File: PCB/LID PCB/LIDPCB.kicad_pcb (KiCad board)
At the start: 2 copper layers, 22 x 17 mm, 10 parts, among them J1 POWER/I2C, U1 LTR-329ALS-01, U2 LSM6DSMTR

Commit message: Main pcb reviewed
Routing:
- net /SDA: track 13.5 -> 18.8 mm
- net /SCL: track 17.5 -> 19.0 mm
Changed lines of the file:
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@@
   (segment (start 115.9 114.3) (end 118.5 114.3) (width 0.25) (layer "B.Cu") (net 2))
   (segment (start 102.75 107.175) (end 102.75 104.2875) (width 0.25) (layer "F.Cu") (net 3))
-  (segment (start 117.1 111.1) (end 117.9 111.1) (width 0.2) (layer "F.Cu") (net 4))
-  (segment (start 117.9 111.1) (end 118 111) (width 0.2) (layer "F.Cu") (net 4))
-  (segment (start 118 111) (end 118 113.34) (width 0.25) (layer "F.Cu") (net 4))
+  (segment (start 118 113.34) (end 118 112.8) (width 0.16) (layer "F.Cu") (net 4))
+  (segment (start 117.1 111.1) (end 117.9 111.1) (width 0.16) (layer "F.Cu") (net 4))
+  (segment (start 117.462476 111.9) (end 117.7 111.9) (width 0.16) (layer "F.Cu") (net 4))
+  (segment (start 117.9 111.1) (end 118 111) (width 0.16) (layer "F.Cu") (net 4))
+  (segment (start 118 111.6) (end 118 111.55) (width 0.16) (layer "F.Cu") (net 4))
+  (segment (start 117.7 112.5) (end 117.462476 112.5) (width 0.16) (layer "F.Cu") (net 4))
+  (segment (start 118 111.55) (end 118 111) (width 0.16) (layer "F.Cu") (net 4))
   (via (at 117.1 111.1) (size 0.5) (drill 0.25) (layers "F.Cu" "B.Cu") (net 4))
-  (segment (start 107.75 109) (end 109.3 110.55) (width 0.2) (layer "B.Cu") (net 4))
-  (segment (start 109.3 110.55) (end 113.7 110.55) (width 0.2) (layer "B.Cu") (net 4))
-  (segment (start 115.915686 110.55) (end 116.332843 110.967157) (width 0.2) (layer "B.Cu") (net 4))
-  (segment (start 116.465686 111.1) (end 117.1 111.1) (width 0.2) (layer "B.Cu") (net 4))
-  (segment (start 116.332843 110.967157) (end 116.465686 111.1) (width 0.2) (layer "B.Cu") (net 4))
-  (segment (start 113.7 110.55) (end 115.915686 110.55) (width 0.2) (layer "B.Cu") (net 4))
-  (segment (start 118.5 111.699998) (end 118.5 113.34) (width 0.25) (layer "F.Cu") (net 5))
-  (segment (start 119.299998 111.1) (end 119.199998 111) (width 0.2) (layer "F.Cu") (net 5))
-  (segment (start 119.199998 111) (end 118.5 111.699998) (width 0.25) (layer "F.Cu") (net 5))
-  (segment (start 120 111.1) (end 119.299998 111.1) (width 0.2) (layer "F.Cu") (net 5))
+  (arc (start 117.162476 112.2) (mid 117.250344 111.987868) (end 117.462476 111.9) (width 0.16) (layer "F.Cu") (net 4))
+  (arc (start 117.462476 112.5) (mid 117.250344 112.412132) (end 117.162476 112.2) (width 0.16) (layer "F.Cu") (net 4))
+  (arc (start 117.7 111.9) (mid 117.912132 111.812132) (end 118 111.6) (width 0.16) (layer "F.Cu") (net 4))
+  (arc (start 118 112.8) (mid 117.912132 112.587868) (end 117.7 112.5) (width 0.16) (layer "F.Cu") (net 4))
+  (segment (start 115.75 110.55) (end 115.8 110.55) (width 0.16) (layer "B.Cu") (net 4))
+  (segment (start 114.25 109.876854) (end 114.25 110.25) (width 0.16) (layer "B.Cu") (net 4))
+  (segment (start 114.85 110.25) (end 114.85 109.876854) (width 0.16) (layer "B.Cu") (net 4))
+  (segment (start 115.915686 110.55) (end 116.465686 111.1) (width 0.16) (layer "B.Cu") (net 4))
+  (segment (start 116.465686 111.1) (end 117.1 111.1) (width 0.16) (layer "B.Cu") (net 4))
+  (segment (start 115.8 110.55) (end 115.915686 110.55) (width 0.16) (layer "B.Cu") (net 4))
+  (segment (start 115.45 109.876854) (end 115.45 110.25) (width 0.16) (layer "B.Cu") (net 4))
+  (segment (start 107.75 109) (end 109.3 110.55) (width 0.16) (layer "B.Cu") (net 4))
+  (segment (start 109.3 110.55) (end 112.15 110.55) (width 0.16) (layer "B.Cu") (net 4))
+  (segment (start 113.05 109.876854) (end 113.05 110.25) (width 0.16) (layer "B.Cu") (net 4))
+  (segment (start 112.45 110.25) (end 112.45 109.876854) (width 0.16) (layer "B.Cu") (net 4))
+  (segment (start 113.65 110.25) (end 113.65 109.876854) (width 0.16) (layer "B.Cu") (net 4))
+  (arc (start 114.85 109.876854) (mid 114.937868 109.664722) (end 115.15 109.576854) (width 0.16) (layer "B.Cu") (net 4))
+  (arc (start 114.25 110.25) (mid 114.337868 110.462132) (end 114.55 110.55) (width 0.16) (layer "B.Cu") (net 4))
+  (arc (start 115.45 110.25) (mid 115.537868 110.462132) (end 115.75 110.55) (width 0.16) (layer "B.Cu") (net 4))
+  (arc (start 113.95 109.576854) (mid 114.162132 109.664722) (end 114.25 109.876854) (width 0.16) (layer "B.Cu") (net 4))
+  (arc (start 112.15 110.55) (mid 112.362132 110.462132) (end 112.45 110.25) (width 0.16) (layer "B.Cu") (net 4))
+  (arc (start 113.65 109.876854) (mid 113.737868 109.664722) (end 113.95 109.576854) (width 0.16) (layer "B.Cu") (net 4))
+  (arc (start 112.75 109.576854) (mid 112.962132 109.664722) (end 113.05 109.876854) (width 0.16) (layer "B.Cu") (net 4))
+  (arc (start 112.45 109.876854) (mid 112.537868 109.664722) (end 112.75 109.576854) (width 0.16) (layer "B.Cu") (net 4))
+  (arc (start 113.05 110.25) (mid 113.137868 110.462132) (end 113.35 110.55) (width 0.16) (layer "B.Cu") (net 4))
+  (arc (start 115.15 109.576854) (mid 115.362132 109.664722) (end 115.45 109.876854) (width 0.16) (layer "B.Cu") (net 4))
+  (arc (start 113.35 110.55) (mid 113.562132 110.462132) (end 113.65 110.25) (width 0.16) (layer "B.Cu") (net 4))
+  (arc (start 114.55 110.55) (mid 114.762132 110.462132) (end 114.85 110.25) (width 0.16) (layer "B.Cu") (net 4))
+  (segment (start 118.5 112.9) (end 118.6302 112.7698) (width 0.16) (layer "F.Cu") (net 5))
+  (segment (start 118.6302 112.7698) (end 118.6302 112.4302) (width 0.16) (layer "F.Cu") (net 5))
+  (segment (start 118.7302 111) (end 119.199998 111) (width 0.16) (layer "F.Cu") (net 5))
+  (segment (start 118.6302 111.1) (end 118.7302 111) (width 0.16) (layer "F.Cu") (net 5))
+  (segment (start 119.299998 111.1) (end 119.199998 111) (width 0.16) (layer "F.Cu") (net 5))
+  (segment (start 118.6302 111.2302) (end 118.6302 111.1) (width 0.16) (layer "F.Cu") (net 5))
+  (segment (start 119.18515 111.87525) (end 119.18515 111.8302) (width 0.16) (layer "F.Cu") (net 5))
+  (segment (start 118.6302 111.27525) (end 118.6302 111.2302) (width 0.16) (layer "F.Cu") (net 5))
+  (segment (start 120 111.1) (end 119.299998 111.1) (width 0.16) (layer "F.Cu") (net 5))
+  (segment (start 118.5 113.34) (end 118.5 112.9) (width 0.16) (layer "F.Cu") (net 5))
   (via (at 120 111.1) (size 0.5) (drill 0.25) (layers "F.Cu" "B.Cu") (net 5))
-  (segment (start 107.75 112) (end 108.8 110.95) (width 0.2) (layer "B.Cu") (net 5))
-  (segment (start 120 111.2) (end 120 111.1) (width 0.2) (layer "B.Cu") (net 5))
-  (segment (start 119.2 112.3) (end 120 111.5) (width 0.2) (layer "B.Cu") (net 5))
-  (segment (start 117.2 112.4) (end 119.1 112.4) (width 0.2) (layer "B.Cu") (net 5))
-  (segment (start 119.1 112.4) (end 119.2 112.3) (width 0.2) (layer "B.Cu") (net 5))
-  (segment (start 120 111.5) (end 120 111.2) (width 0.2) (layer "B.Cu") (net 5))
-  (segment (start 108.8 110.95) (end 115.75 110.95) (width 0.2) (layer "B.Cu") (net 5))
-  (segment (start 115.75 110.95) (end 117.2 112.4) (width 0.2) (layer "B.Cu") (net 5))
+  (arc (start 118.907675 112.152725) (mid 119.103879 112.071454) (end 119.18515 111.87525) (width 0.16) (layer "F.Cu") (net 5))
+  (arc (start 118.6302 112.4302) (mid 118.711471 112.233996) (end 118.907675 112.152725) (width 0.16) (layer "F.Cu") (net 5))
+  (arc (start 119.18515 111.8302) (mid 119.103879 111.633996) (end 118.907675 111.552725) (width 0.16) (layer "F.Cu") (net 5))
+  (arc (start 118.907675 111.552725) (mid 118.711471 111.471454) (end 118.6302 111.27525) (width 0.16) (layer "F.Cu") (net 5))
+  (segment (start 119.1 112.4) (end 117.2 112.4) (width 0.16) (layer "B.Cu") (net 5))
+  (segment (start 117.2 112.4) (end 115.75 110.95) (width 0.16) (layer "B.Cu") (net 5))
+  (segment (start 112.91485 111.485151) (end 112.85 111.485151) (width 0.16) (layer "B.Cu") (net 5))
+  (segment (start 108.8 110.95) (end 107.75 112) (width 0.16) (layer "B.Cu") (net 5))
+  (segment (start 115.75 110.95) (end 113.45 110.95) (width 0.16) (layer "B.Cu") (net 5))
+  (segment (start 112.25 110.95) (end 108.8 110.95) (width 0.16) (layer "B.Cu") (net 5))
+  (segment (start 112.582425 111.217576) (end 112.582425 111.217575) (width 0.16) (layer "B.Cu") (net 5))
+  (segment (start 113.182425 111.217575) (end 113.182425 111.217576) (width 0.16) (layer "B.Cu") (net 5))
+  (segment (start 112.31485 110.95) (end 112.25 110.95) (width 0.16) (layer "B.Cu") (net 5))
+  (segment (start 120 111.5) (end 119.1 112.4) (width 0.16) (layer "B.Cu") (net 5))
+  (segment (start 120 111.1) (end 120 111.5) (width 0.16) (layer "B.Cu") (net 5))
+  (arc (start 112.85 111.485151) (mid 112.660796 111.40678) (end 112.582425 111.217576) (width 0.16) (layer "B.Cu") (net 5))
+  (arc (start 112.582425 111.217575) (mid 112.504054 111.028371) (end 112.31485 110.95) (width 0.16) (layer "B.Cu") (net 5))
+  (arc (start 113.182425 111.217576) (mid 113.104054 111.40678) (end 112.91485 111.485151) (width 0.16) (layer "B.Cu") (net 5))
+  (arc (start 113.45 110.95) (mid 113.260796 111.028371) (end 113.182425 111.217575) (width 0.16) (layer "B.Cu") (net 5))
   (zone (net 2) (net_name "GND") (layers F&B.Cu) (hatch edge 0.508)
     (priority 1)

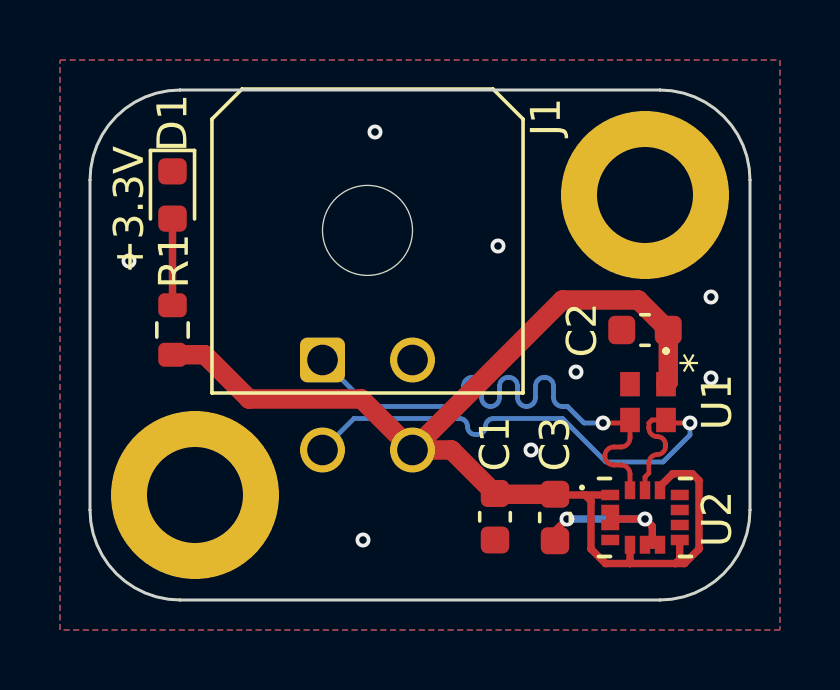
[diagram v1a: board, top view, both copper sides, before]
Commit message: 3x PCB ready for gerberization
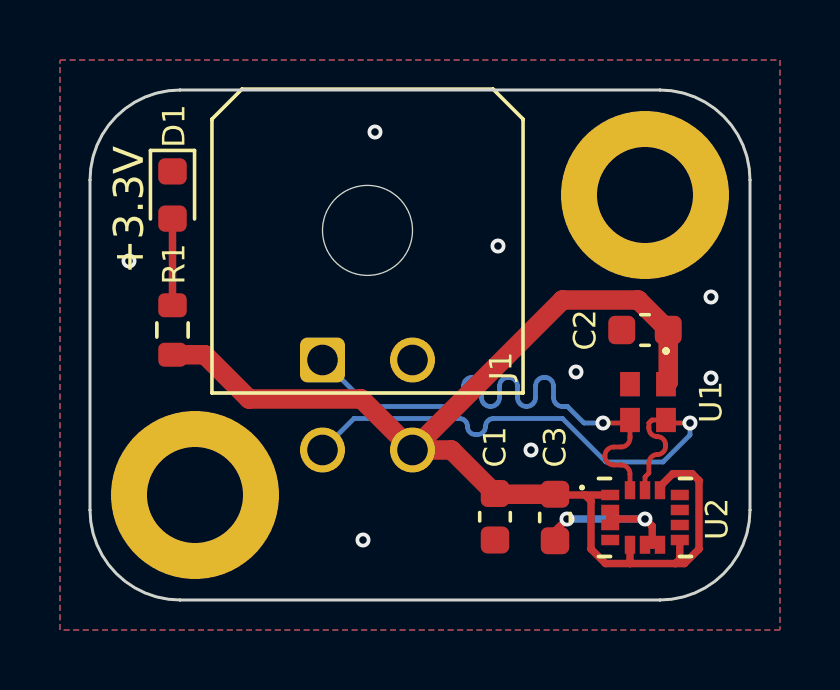
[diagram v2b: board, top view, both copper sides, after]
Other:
- board text added: "22x17mm H M3x10x15mm"
- board text removed: "H M3x10x15mm"
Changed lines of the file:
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@@
     (attr exclude_from_pos_files)
     (fp_text reference "H2" (at 0 -3.8) (layer "F.SilkS") hide
-      (effects (font (size 1 1) (thickness 0.16)))
+      (effects (font (size 0.75 0.75) (thickness 0.15)))
     )
     (fp_text value "MountingHole" (at 0 3.8) (layer "F.Fab")
@@
     (property "Vendor Part Number" "1276-1935-1-ND")
     (attr smd)
-    (fp_text reference "C3" (at 2.45 0 90) (layer "F.SilkS")
-      (effects (font (size 1 1) (thickness 0.16)))
+    (fp_text reference "C3" (at 2.35 0 90) (layer "F.SilkS")
+      (effects (font (size 0.75 0.75) (thickness 0.15)))
     )
     (fp_text value "0.1 uF 50V X7R 0603" (at 0 1.43 90) (layer "F.Fab")
@@
     (property "Vendor Part Number" "1276-1102-1-ND")
     (attr smd)
-    (fp_text reference "C1" (at -2.425 0 90) (layer "F.SilkS")
-      (effects (font (size 1 1) (thickness 0.16)))
+    (fp_text reference "C1" (at -2.325 0 90) (layer "F.SilkS")
+      (effects (font (size 0.75 0.75) (thickness 0.15)))
     )
     (fp_text value "1 uF 25V X5R 0603" (at 0 1.43 90) (layer "F.Fab")
@@
     (attr smd)
     (fp_text reference "U2" (at 2.4 0.05 90) (layer "F.SilkS")
-      (effects (font (size 1 1) (thickness 0.16)))
+      (effects (font (size 0.75 0.75) (thickness 0.15)))
     )
     (fp_text value "LSM6DSMTR" (at 4.9008 1.9952) (layer "F.Fab")
@@
     (property "Vendor Part Number" "160-2160-1-ND")
     (attr through_hole)
-    (fp_text reference "U1" (at 0 -2.300001 -90) (layer "F.SilkS")
-      (effects (font (size 1 1) (thickness 0.16)))
+    (fp_text reference "U1" (at -0.0031 -2.100001 -90) (layer "F.SilkS")
+      (effects (font (size 0.75 0.75) (thickness 0.15)))
     )
     (fp_text value "LTR-329ALS-01" (at 0 0 90) (layer "F.SilkS") hide
       (effects (font (size 1 1) (thickness 0.15)))
     )
-    (fp_text user "*" (at -1.3031 -1.600001 90) (layer "F.SilkS")
+    (fp_text user "*" (at -1.3031 -1.600001 90) (layer "F.SilkS") hide
       (effects (font (size 1 1) (thickness 0.15)))
     )
@@
     (property "Vendor Part Number" "1276-1935-1-ND")
     (attr smd)
-    (fp_text reference "C2" (at -2.1 0 90) (layer "F.SilkS")
-      (effects (font (size 1 1) (thickness 0.16)))
+    (fp_text reference "C2" (at -2 0 90) (layer "F.SilkS")
+      (effects (font (size 0.75 0.75) (thickness 0.15)))
     )
     (fp_text value "0.1 uF 50V X7R 0603" (at 0 1.43) (layer "F.Fab")
@@
     (property "Vendor Part Number" "846-CSL1901UW1CT-ND")
     (attr smd)
-    (fp_text reference "D1" (at -2.4 0 90) (layer "F.SilkS")
-      (effects (font (size 1 1) (thickness 0.16)))
+    (fp_text reference "D1" (at -2.3 -0.05 90) (layer "F.SilkS")
+      (effects (font (size 0.75 0.75) (thickness 0.15)))
     )
     (fp_text value "RED 1.8V 2mA 0603" (at 0 1.43 90) (layer "F.Fab")
@@
     (attr exclude_from_pos_files)
     (fp_text reference "H1" (at 0 -3.8) (layer "F.SilkS") hide
-      (effects (font (size 1 1) (thickness 0.16)))
+      (effects (font (size 0.75 0.75) (thickness 0.15)))
     )
     (fp_text value "MountingHole" (at 0 3.8) (layer "F.Fab")
@@
     (property "Vendor Part Number" "311-750HRCT-ND")
     (attr smd)
-    (fp_text reference "R1" (at -2.3 -0.05 90) (layer "F.SilkS")
-      (effects (font (size 1 1) (thickness 0.16)))
+    (fp_text reference "R1" (at -2.2 -0.05 90) (layer "F.SilkS")
+      (effects (font (size 0.75 0.75) (thickness 0.15)))
     )
     (fp_text value "750Ohm 1% 0603" (at 0 1.43 90) (layer "F.Fab")
@@
     (property "Vendor Part Number" "WM1814-ND")
     (attr through_hole)
-    (fp_text reference "J1" (at 7.45 -8.1 90) (layer "F.SilkS")
-      (effects (font (size 1 1) (thickness 0.16)))
+    (fp_text reference "J1" (at 5.95 0.2 90) (layer "F.SilkS")
+      (effects (font (size 0.75 0.75) (thickness 0.15)))
     )
     (fp_text value "POWER/I2C" (at 1.5 5.7) (layer "F.Fab")
@@
     (effects (font (size 1.5 1.5) (thickness 0.3)) (justify mirror))
   )
-  (gr_text "H M3x10x15mm" (at 107.1 101.4) (layer "B.SilkS")
+  (gr_text "22x17mm\nH M3x10x15mm" (at 106.9 102) (layer "B.SilkS")
     (effects (font (size 1 1) (thickness 0.16)) (justify mirror))
   )
